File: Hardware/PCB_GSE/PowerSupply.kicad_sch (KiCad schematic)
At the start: 47 parts, among them J8 Vin_XT30PW-F, U1 L6981N33DR, U3 MPQ9843GLE-5-AEC1-Z

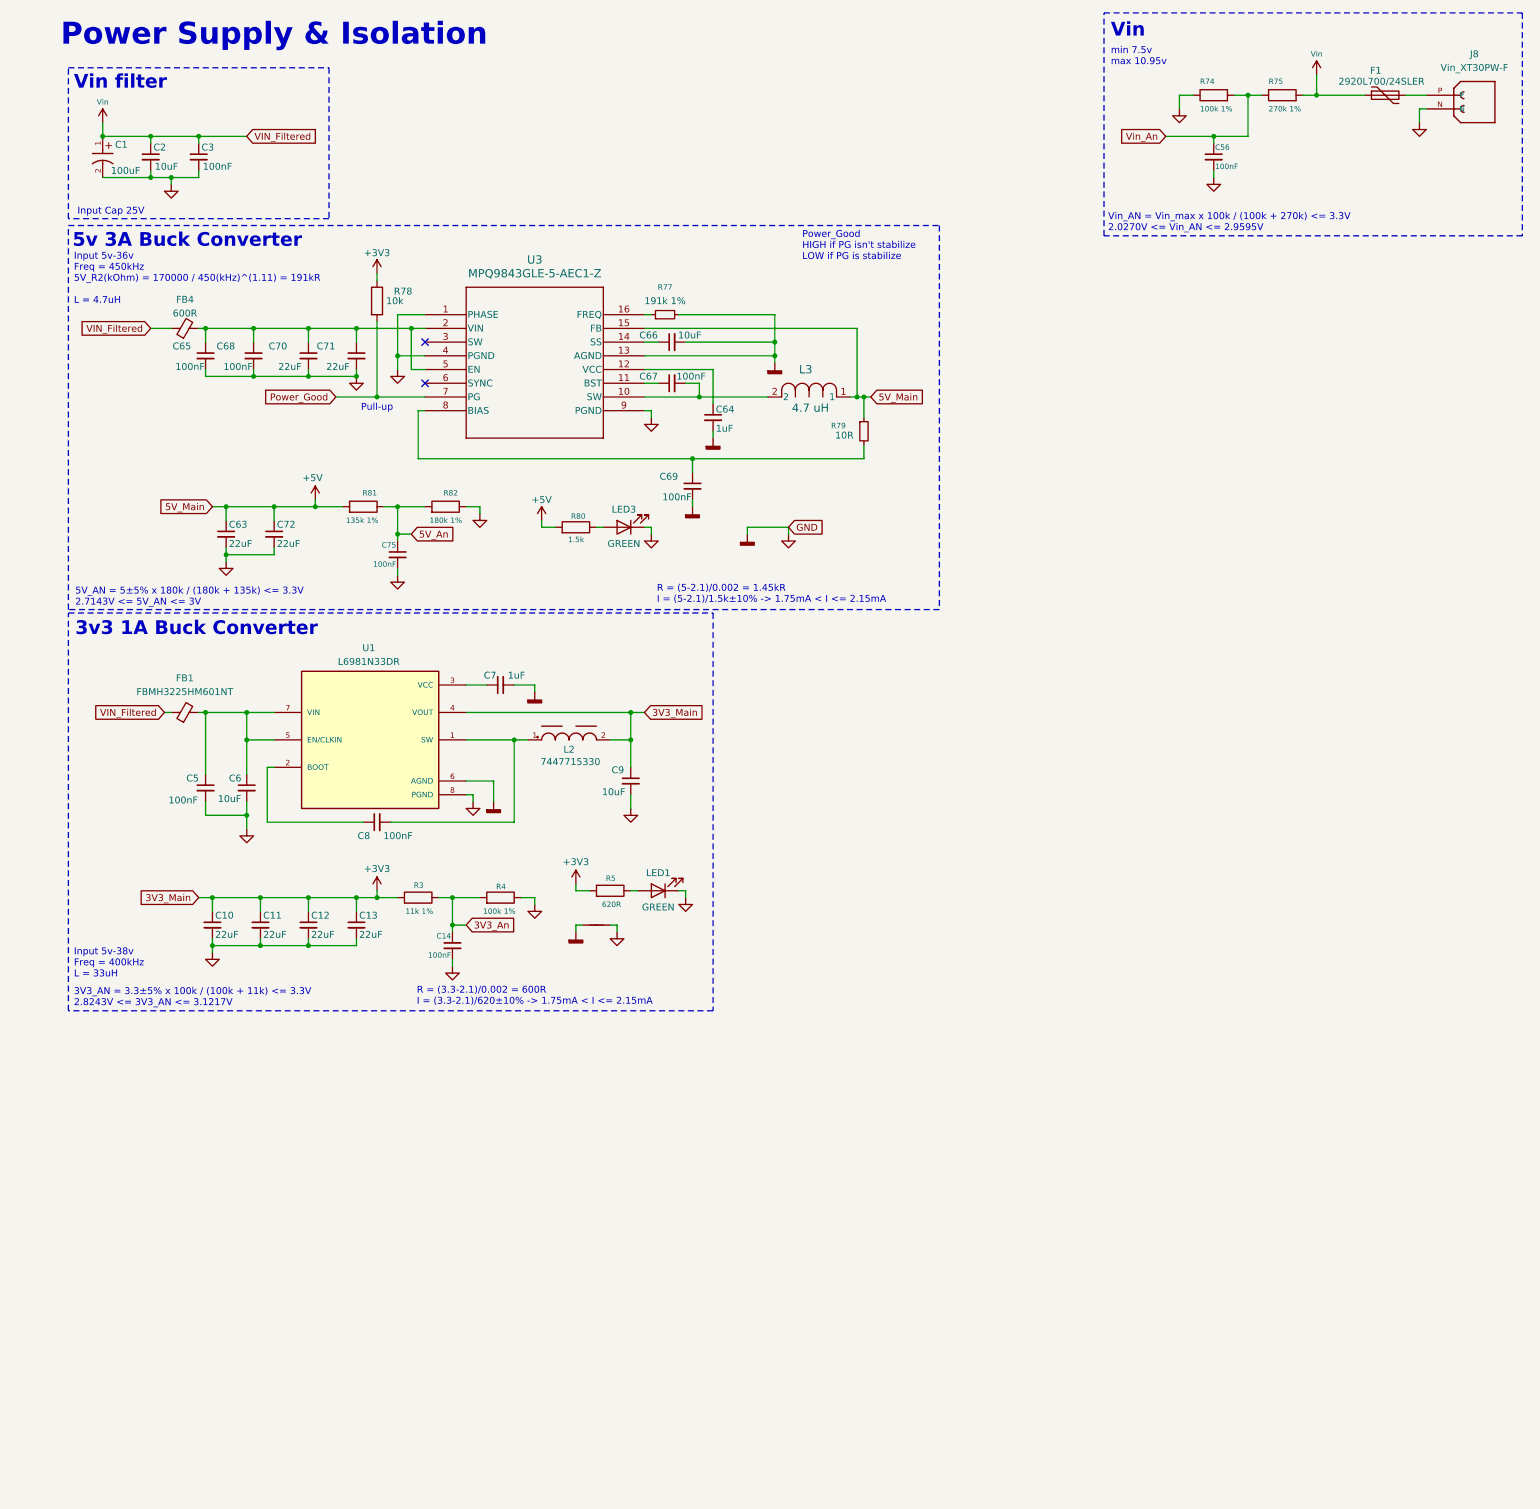
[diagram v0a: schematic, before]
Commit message: feat: add 12V buck converter + inductance symbol/footprint
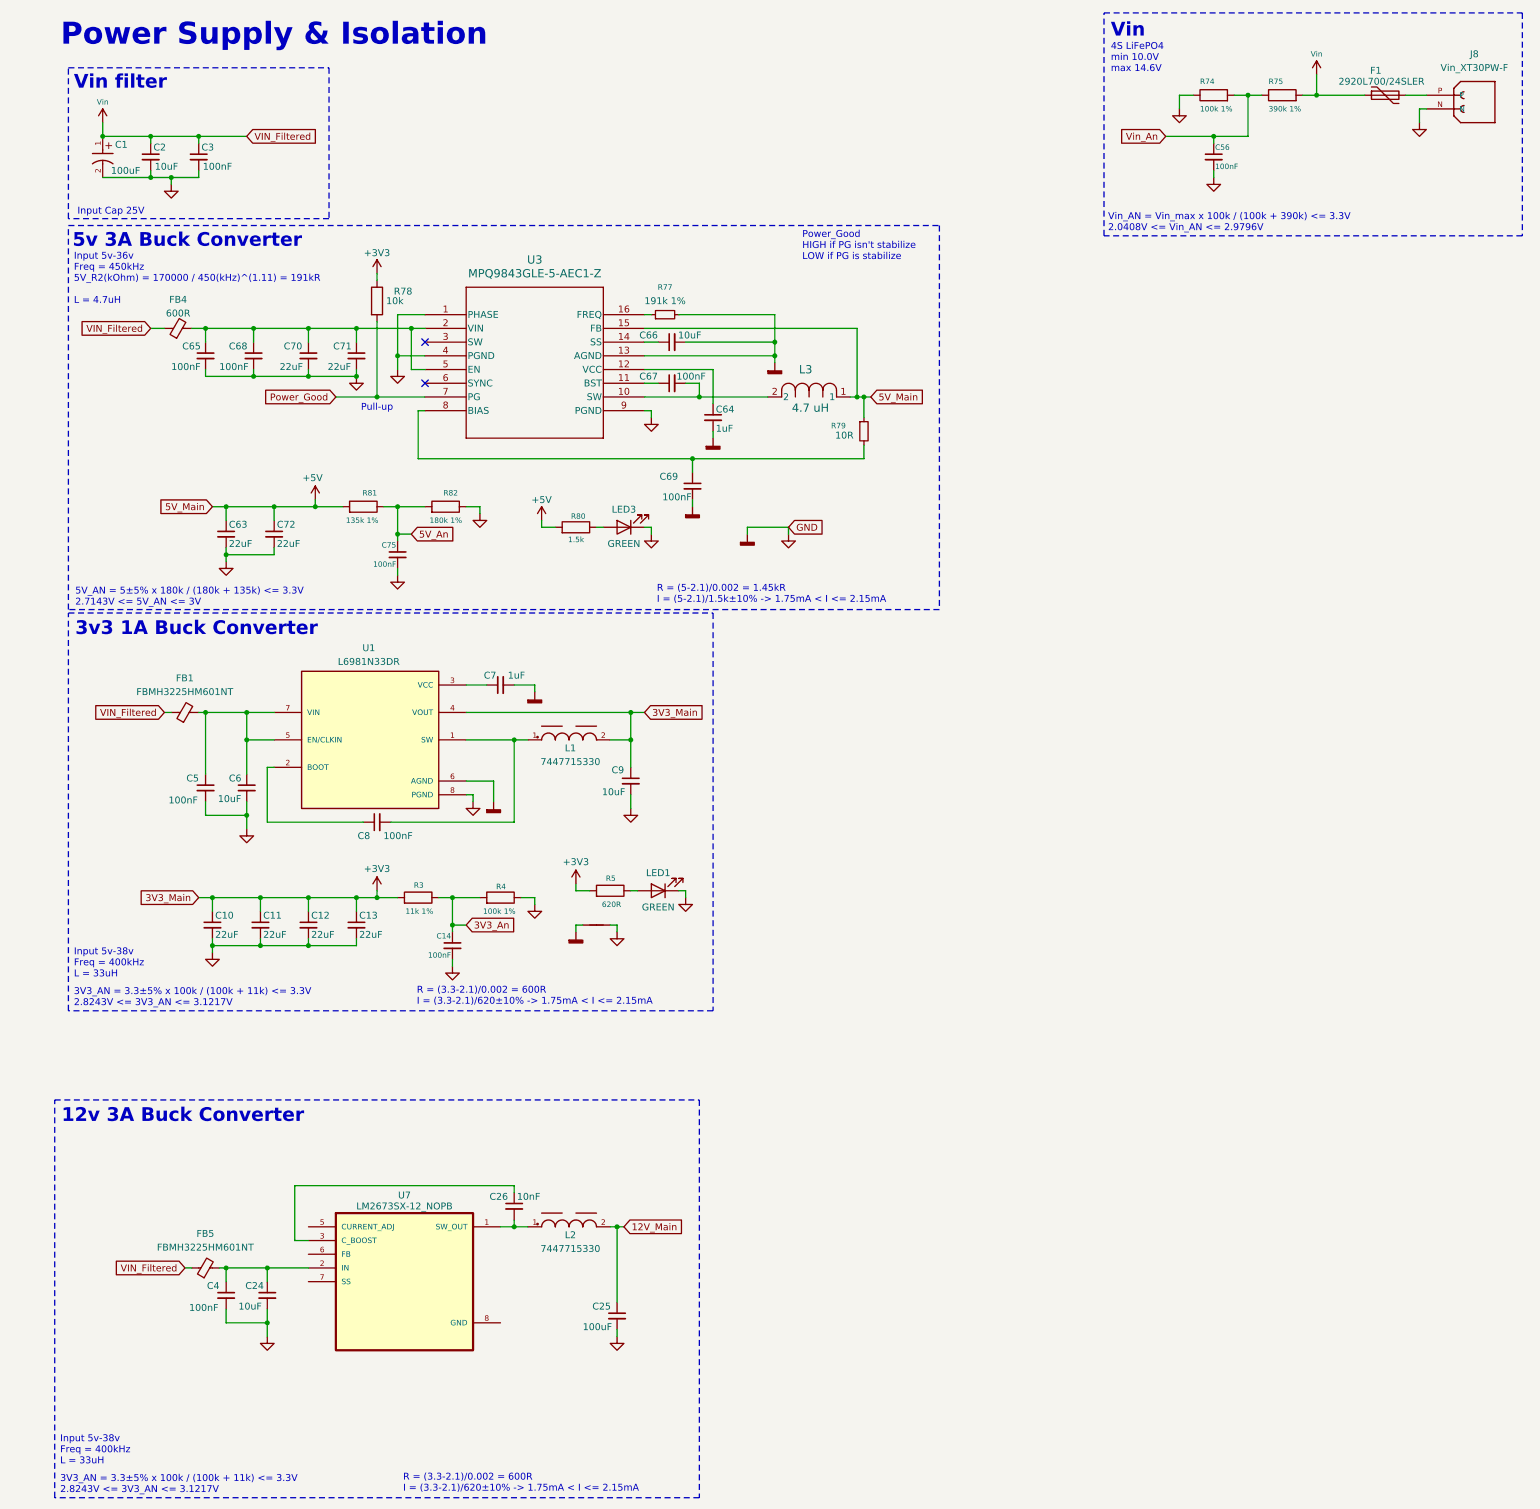
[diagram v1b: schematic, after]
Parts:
- removed L2: 7447715330, pcb_moteur:WE-PD_1245, symbol ODB2:WE-PD_1245
- added C24: 10uF, Capacitor_SMD:C_0805_2012Metric, symbol Device:C_Small
- added C25: 100uF, Capacitor_SMD:C_0805_2012Metric, symbol Device:C_Small
- added C26: 10nF, Capacitor_SMD:C_0805_2012Metric, symbol Device:C_Small
- added C4: 100nF, Capacitor_SMD:C_0805_2012Metric, symbol Device:C_Small
- added FB5: FBMH3225HM601NT, Inductor_SMD:L_1210_3225Metric, symbol Device:FerriteBead_Small
- added L1, L2: 7447715330, WE-PD_1245:WE-PD_1245, symbol PCB_GSE:WE-PD_1245
- added U7: LM2673SX-12_NOPB, LM2673SX-12_NOPB:TO127P1435X464-8N, symbol PCB_GSE:LM2673SX-12_NOPB
- R75: value 270k 1% -> 390k 1%
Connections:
- net +3V3: now also L1.2
- net AGND5V: now also C24.2, C25.2, C4.2, U7.4 (GND), U7.8 (GND)
- net Vin: now also FB5.1
- net at C8.2, U1.1 (SW): now also L1.1
- new net: C26.2, L2.1, U7.1 (SW_OUT)
- new net: C24.1, C4.1, FB5.2, U7.2 (IN)
- new net: C26.1, U7.3 (C_BOOST)
- new net 12V_Main: C25.1, L2.2
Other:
- note added: "12v 3A Buck Converter"
- note added: "4S LiFePO4 min 10.0V max 14.6V"
- note added: "Vin_AN = Vin_max x 100k / (100k + 390k) <= 3.3V 2.0408V <= Vin_AN <= 2.9796V"
- note removed: "Vin_AN = Vin_max x 100k / (100k + 270k) <= 3.3V 2.0270V <= Vin_AN <= 2.9595V"
- note removed: "min 7.5v max 10.95v"
- moved on the sheet: FB4

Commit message: feat: finish 12V-3A buck converter
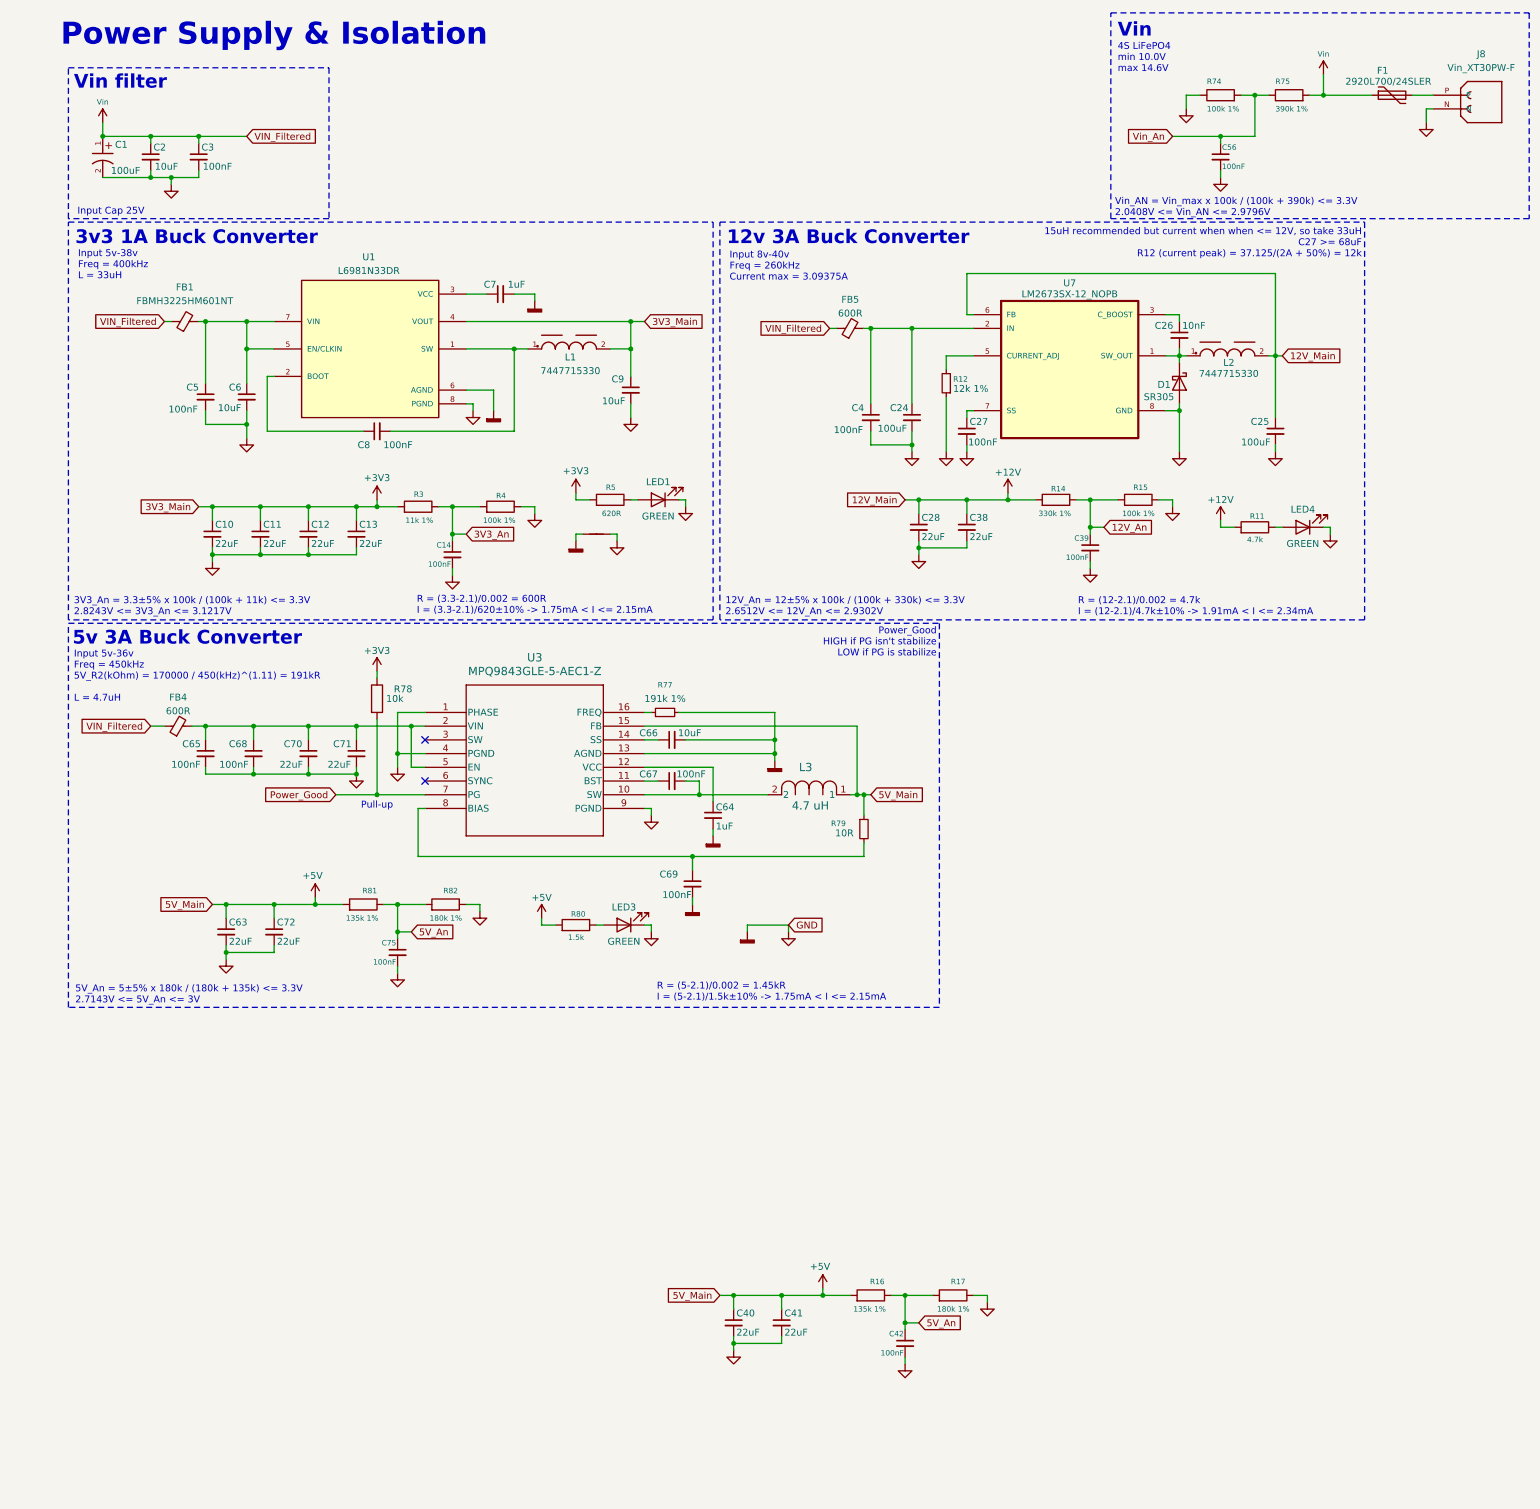
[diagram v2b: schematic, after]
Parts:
- added C27: 100nF, Capacitor_SMD:C_0805_2012Metric, symbol Device:C_Small
- added C28, C38, C40, C41: 22uF, Capacitor_SMD:C_0805_2012Metric, symbol Device:C_Small
- added C39, C42: 100nF, ODB:C_0402_1005Metric, symbol Device:C_Small
- added D1: SR305, symbol Device:D_Schottky
- added LED4: GREEN, ODB:LED_QBLP601-AG15, symbol Device:LED
- added R11: 4.7k, Resistor_SMD:R_0603_1608Metric, symbol Device:R
- added R12: 12k 1%, Resistor_SMD:R_0603_1608Metric, symbol Device:R_Small
- added R14: 330k 1%, Resistor_SMD:R_0603_1608Metric, symbol Device:R
- added R15: 100k 1%, Resistor_SMD:R_0603_1608Metric, symbol Device:R
- added R16: 135k 1%, Resistor_SMD:R_0603_1608Metric, symbol Device:R
- added R17: 180k 1%, Resistor_SMD:R_0603_1608Metric, symbol Device:R
- C24: value 10uF -> 100uF
- FB5: value FBMH3225HM601NT -> 600R; DigiKey_Part_Number (none) -> 587-1755-1-ND; Manufacturer_Part_Number (none) -> FBMH3225HM601NT
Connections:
- net 12V_Main is gone; now on net +12V: C25.1, L2.2
- net +5V: now also C40.1, C41.1, R16.2
- net 5V_An: now also C42.1, R16.1, R17.2
- net AGND5V: now also C27.2, C28.2, C38.2, C39.2, C40.2, C41.2, C42.2, D1.2 (A), LED4.1 (K), R12.1, R15.1, R17.1
- net at C26.2, L2.1, U7.1 (SW_OUT): now also D1.1 (K)
- net at U7.5 (CURRENT_ADJ): now also R12.2
- net +12V: now reaches U7.6 (FB)
- net +12V: now also C28.1, C38.1, R11.2, R14.2
- net at U7.7 (SS): now also C27.1
- new net: LED4.2 (A), R11.1
- new net 12V_An: C39.1, R14.1, R15.2
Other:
- note added: "12V_An = 12±5% x 100k / (100k + 330k) <= 3.3V 2.6512V <= 12V_An <= 2.9302V"
- note added: "15uH recommended but current when when <= 12V, so take 33uH C27 >= 68uF R12 (current peak) = 37.125/(2A + 50%) = 12k"
- note added: "3V3_An = 3.3±5% x 100k / (100k + 11k) <= 3.3V 2.8243V <= 3V3_An <= 3.1217V"
- note added: "5V_An = 5±5% x 180k / (180k + 135k) <= 3.3V 2.7143V <= 5V_An <= 3V"
- note added: "Input 8v-40v Freq = 260kHz Current max = 3.09375A"
- note added: "R = (12-2.1)/0.002 = 4.7k I = (12-2.1)/4.7k±10% -> 1.91mA < I <= 2.34mA"
- note removed: "3V3_AN = 3.3±5% x 100k / (100k + 11k) <= 3.3V 2.8243V <= 3V3_AN <= 3.1217V"
- note removed: "5V_AN = 5±5% x 180k / (180k + 135k) <= 3.3V 2.7143V <= 5V_AN <= 3V"
- moved on the sheet: C10, C11, C12, C13, C14, C24, C25, C26, C4, C5, C56, C6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

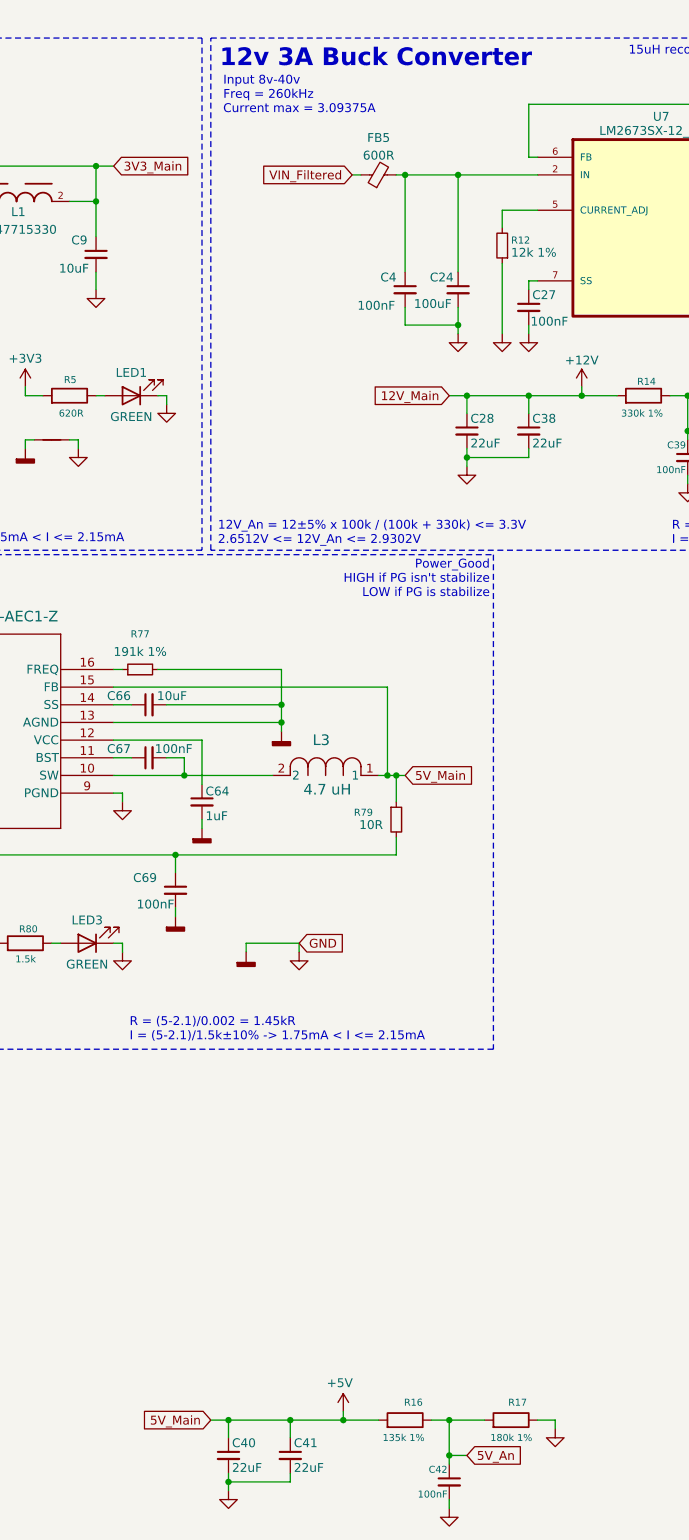
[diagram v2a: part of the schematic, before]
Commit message: fix: add ferritbead + remove typos
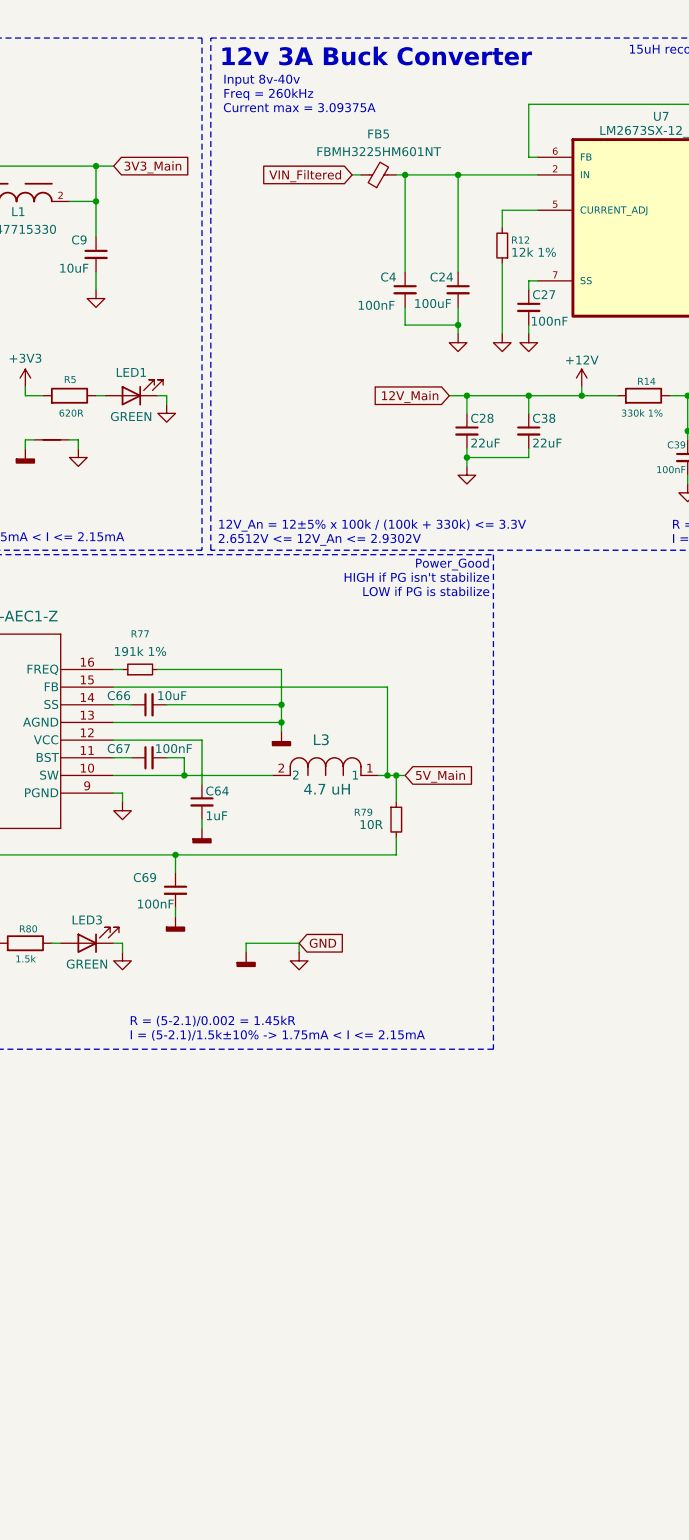
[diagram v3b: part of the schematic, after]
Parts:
- removed C40, C41: 22uF, Capacitor_SMD:C_0805_2012Metric, symbol Device:C_Small
- removed C42: 100nF, ODB:C_0402_1005Metric, symbol Device:C_Small
- removed R16: 135k 1%, Resistor_SMD:R_0603_1608Metric, symbol Device:R
- removed R17: 180k 1%, Resistor_SMD:R_0603_1608Metric, symbol Device:R
- FB5: value 600R -> FBMH3225HM601NT; DigiKey_Part_Number 587-1755-1-ND -> (none); Manufacturer_Part_Number FBMH3225HM601NT -> (none)
